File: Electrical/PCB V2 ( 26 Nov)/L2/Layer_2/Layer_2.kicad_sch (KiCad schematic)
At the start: 13 parts, among them SW1 SW_Push, U1 LM2596ADJ, U2 LM2596ADJ, U3 XT30UPB-M, U4 XT30UPB-M, U5 ESP32-S3-DEVKITM-1-N8, U6 XT30UPB-M, U7 XT30UPB-M, U8 XT30UPB-M, U9 XT30UPB-M

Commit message: ye
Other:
- note added: "Motor Controllers"
- note removed: "Motors"
- moved on the sheet: U3, U4, U5
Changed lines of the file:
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@@
 	)
 	(rectangle
-		(start 144.78 66.04)
-		(end 195.58 134.62)
+		(start 198.12 19.05)
+		(end 248.92 87.63)
 		(stroke
 			(width 0)
@@
 	)
 	(rectangle
-		(start 96.52 127)
-		(end 139.7 147.32)
+		(start 90.17 73.66)
+		(end 133.35 93.98)
 		(stroke
 			(width 0)
@@
 	(text "Coonector thing\n"
 		(exclude_from_sim no)
-		(at 116.586 122.936 0)
+		(at 110.236 69.596 0)
 		(effects
 			(font
@@
 		)
 	)
-	(text "Motors\n"
+	(text "Motor Controllers\n"
 		(exclude_from_sim no)
 		(at 130.556 20.828 0)
@@
 	(text "ESP32 for motor control\n"
 		(exclude_from_sim no)
-		(at 211.836 92.202 0)
+		(at 265.176 45.212 0)
 		(effects
 			(font
@@
 	)
 	(label "IN6"
-		(at 152.4 91.44 0)
+		(at 205.74 44.45 0)
 		(fields_autoplaced yes)
 		(effects
@@
 	)
 	(label "GND"
-		(at 152.4 129.54 0)
+		(at 205.74 82.55 0)
 		(fields_autoplaced yes)
 		(effects
@@
 	)
 	(label "IN8"
-		(at 152.4 96.52 0)
+		(at 205.74 49.53 0)
 		(fields_autoplaced yes)
 		(effects
@@
 	)
 	(label "IN1"
-		(at 152.4 78.74 0)
+		(at 205.74 31.75 0)
 		(fields_autoplaced yes)
 		(effects
@@
 	)
 	(label "3v3"
-		(at 152.4 76.2 0)
+		(at 205.74 29.21 0)
 		(fields_autoplaced yes)
 		(effects
@@
 	)
 	(label "3v3"
-		(at 133.35 138.43 0)
+		(at 127 85.09 0)
 		(fields_autoplaced yes)
 		(effects
@@
 	)
 	(label "IN7"
-		(at 152.4 93.98 0)
+		(at 205.74 46.99 0)
 		(fields_autoplaced yes)
 		(effects
@@
 	)
 	(label "GND"
-		(at 133.35 140.97 0)
+		(at 127 87.63 0)
 		(fields_autoplaced yes)
 		(effects
@@
 	)
 	(label "IN2"
-		(at 152.4 81.28 0)
+		(at 205.74 34.29 0)
 		(fields_autoplaced yes)
 		(effects
@@
 	)
 	(label "5v"
-		(at 114.3 139.7 0)
+		(at 107.95 86.36 0)
 		(fields_autoplaced yes)
 		(effects
@@
 	)
 	(label "IN3"
-		(at 152.4 83.82 0)
+		(at 205.74 36.83 0)
 		(fields_autoplaced yes)
 		(effects
@@
 	)
 	(label "GND"
-		(at 114.3 142.24 0)
+		(at 107.95 88.9 0)
 		(fields_autoplaced yes)
 		(effects
@@
 	)
 	(label "IN4"
-		(at 152.4 86.36 0)
+		(at 205.74 39.37 0)
 		(fields_autoplaced yes)
 		(effects
@@
 	)
 	(label "IN5"
-		(at 152.4 88.9 0)
+		(at 205.74 41.91 0)
 		(fields_autoplaced yes)
 		(effects
@@
 	(symbol
 		(lib_id "XT30UPB-M:XT30UPB-M")
-		(at 125.73 140.97 0)
+		(at 119.38 87.63 0)
 		(unit 1)
 		(exclude_from_sim no)
@@
 		(fields_autoplaced yes)
 		(property "Reference" "U4"
-			(at 126.365 130.81 0)
+			(at 120.015 77.47 0)
 			(effects
 				(font
@@
 		)
 		(property "Value" "XT30UPB-M"
-			(at 126.365 133.35 0)
+			(at 120.015 80.01 0)
 			(effects
 				(font
@@
 		)
 		(property "Footprint" "XT30UPB-M:XT30UPB-M"
-			(at 125.73 140.97 0)
+			(at 119.38 87.63 0)
 			(effects
 				(font
@@
 		)
 		(property "Datasheet" ""
-			(at 125.73 140.97 0)
+			(at 119.38 87.63 0)
 			(effects
 				(font
@@
 		)
 		(property "Description" ""
-			(at 125.73 140.97 0)
+			(at 119.38 87.63 0)
 			(effects
 				(font
@@
 		)
 		(property "MF" "amass"
-			(at 125.73 140.97 0)
+			(at 119.38 87.63 0)
 			(effects
 				(font
@@
 		)
 		(property "Description_1" "\n                        \n                            Socket; DC supply; XT30; male; PIN: 2; on PCBs; THT; yellow; 15A; 500V\n                        \n"
-			(at 125.73 140.97 0)
+			(at 119.38 87.63 0)
 			(effects
 				(font
@@
 		)
 		(property "Package" "None"
-			(at 125.73 140.97 0)
+			(at 119.38 87.63 0)
 			(effects
 				(font
@@
 		)
 		(property "Price" "None"
-			(at 125.73 140.97 0)
+			(at 119.38 87.63 0)
 			(effects
 				(font
@@
 		)
 		(property "SnapEDA_Link" "https://www.snapeda.com/parts/XT30UPB-M/AMASS/view-part/?ref=snap"
-			(at 125.73 140.97 0)
+			(at 119.38 87.63 0)
 			(effects
 				(font
@@
 		)
 		(property "MP" "XT30UPB-M"
-			(at 125.73 140.97 0)
+			(at 119.38 87.63 0)
 			(effects
 				(font
@@
 		)
 		(property "Availability" "Not in stock"
-			(at 125.73 140.97 0)
+			(at 119.38 87.63 0)
 			(effects
 				(font
@@
 		)
 		(property "Check_prices" "https://www.snapeda.com/parts/XT30UPB-M/AMASS/view-part/?ref=eda"
-			(at 125.73 140.97 0)
+			(at 119.38 87.63 0)
 			(effects
 				(font
@@
 	(symbol
 		(lib_id "ESP32-S3-DEVKITM-1-N8:ESP32-S3-DEVKITM-1-N8")
-		(at 172.72 104.14 0)
+		(at 226.06 57.15 0)
 		(unit 1)
 		(exclude_from_sim no)
@@
 		(fields_autoplaced yes)
 		(property "Reference" "U5"
-			(at 172.72 68.58 0)
+			(at 226.06 21.59 0)
 			(effects
 				(font
@@
 		)
 		(property "Value" "ESP32-S3-DEVKITM-1-N8"
-			(at 172.72 71.12 0)
+			(at 226.06 24.13 0)
 			(effects
 				(font
@@
 		)
 		(property "Footprint" "ESP32-S3-DEVKITM-1-N8:MODULE_ESP32-S3-DEVKITM-1-N8"
-			(at 172.72 104.14 0)
+			(at 226.06 57.15 0)
 			(effects
 				(font
@@
 		)
 		(property "Datasheet" ""
-			(at 172.72 104.14 0)
+			(at 226.06 57.15 0)
 			(effects
 				(font
@@
 		)
 		(property "Description" ""
-			(at 172.72 104.14 0)
+			(at 226.06 57.15 0)
 			(effects
 				(font
@@
 		)
 		(property "MF" "Espressif Systems"
-			(at 172.72 104.14 0)
+			(at 226.06 57.15 0)
 			(effects
 				(font
@@
 		)
 		(property "Description_1" "\n                        \n                            ESP32-S3-MINI-1-N8 ESP32-S Transceiver; 802.11 b/g/n (Wi-Fi, WiFi, WLAN), Bluetooth® 5.x (BLE) 2.4GHz Evaluation Board\n                        \n"
-			(at 172.72 104.14 0)
+			(at 226.06 57.15 0)
 			(effects
 				(font
@@
 		)
 		(property "Package" "None"
-			(at 172.72 104.14 0)
+			(at 226.06 57.15 0)
 			(effects
 				(font
@@
 		)
 		(property "Price" "None"
-			(at 172.72 104.14 0)
+			(at 226.06 57.15 0)
 			(effects
 				(font
@@
 		)
 		(property "Check_prices" "https://www.snapeda.com/parts/ESP32-S3-DEVKITM-1-N8/Espressif+Systems/view-part/?ref=eda"
-			(at 172.72 104.14 0)
+			(at 226.06 57.15 0)
 			(effects
 				(font
@@
 		)
 		(property "STANDARD" "Manufacturer Recommendations"
-			(at 172.72 104.14 0)
+			(at 226.06 57.15 0)
 			(effects
 				(font
@@
 		)
 		(property "PARTREV" "1.0"
-			(at 172.72 104.14 0)
+			(at 226.06 57.15 0)
 			(effects
 				(font
@@
 		)
 		(property "SnapEDA_Link" "https://www.snapeda.com/parts/ESP32-S3-DEVKITM-1-N8/Espressif+Systems/view-part/?ref=snap"
-			(at 172.72 104.14 0)
+			(at 226.06 57.15 0)
 			(effects
 				(font
@@
 		)
 		(property "MP" "ESP32-S3-DEVKITM-1-N8"
-			(at 172.72 104.14 0)
+			(at 226.06 57.15 0)
 			(effects
 				(font
@@
 		)
 		(property "Availability" "In Stock"
-			(at 172.72 104.14 0)
+			(at 226.06 57.15 0)
 			(effects
 				(font
@@
 		)
 		(property "MANUFACTURER" "Espressif Systems"
-			(at 172.72 104.14 0)
+			(at 226.06 57.15 0)
 			(effects
 				(font
@@
 	)
 	(symbol
-		(lib_name "motor driver:L298N")
 		(lib_id "motor driver:L298N")
 		(at 101.6 53.34 0)
@@
 	(symbol
 		(lib_id "XT30UPB-M:XT30UPB-M")
-		(at 106.68 142.24 0)
+		(at 100.33 88.9 0)
 		(unit 1)
 		(exclude_from_sim no)
@@
 		(fields_autoplaced yes)
 		(property "Reference" "U3"
-			(at 107.315 132.08 0)
+			(at 100.965 78.74 0)
 			(effects
 				(font
@@
 		)
 		(property "Value" "XT30UPB-M"
-			(at 107.315 134.62 0)
+			(at 100.965 81.28 0)
 			(effects
 				(font
@@
 		)
 		(property "Footprint" "XT30UPB-M:XT30UPB-M"
-			(at 106.68 142.24 0)
+			(at 100.33 88.9 0)
 			(effects
 				(font
@@
 		)
 		(property "Datasheet" ""
-			(at 106.68 142.24 0)
+			(at 100.33 88.9 0)
 			(effects
 				(font
@@
 		)
 		(property "Description" ""
-			(at 106.68 142.24 0)
+			(at 100.33 88.9 0)
 			(effects
 				(font
@@
 		)
 		(property "MF" "amass"
-			(at 106.68 142.24 0)
+			(at 100.33 88.9 0)
 			(effects
 				(font
@@
 		)
 		(property "Description_1" "\n                        \n                            Socket; DC supply; XT30; male; PIN: 2; on PCBs; THT; yellow; 15A; 500V\n                        \n"
-			(at 106.68 142.24 0)
+			(at 100.33 88.9 0)
 			(effects
 				(font
@@
 		)
 		(property "Package" "None"
-			(at 106.68 142.24 0)
+			(at 100.33 88.9 0)
 			(effects
 				(font
@@
 		)
 		(property "Price" "None"
-			(at 106.68 142.24 0)
+			(at 100.33 88.9 0)
 			(effects
 				(font
@@
 		)
 		(property "SnapEDA_Link" "https://www.snapeda.com/parts/XT30UPB-M/AMASS/view-part/?ref=snap"
-			(at 106.68 142.24 0)
+			(at 100.33 88.9 0)
 			(effects
 				(font
@@
 		)
 		(property "MP" "XT30UPB-M"
-			(at 106.68 142.24 0)
+			(at 100.33 88.9 0)
 			(effects
 				(font
@@
 		)
 		(property "Availability" "Not in stock"
-			(at 106.68 142.24 0)
+			(at 100.33 88.9 0)
 			(effects
 				(font
@@
 		)
 		(property "Check_prices" "https://www.snapeda.com/parts/XT30UPB-M/AMASS/view-part/?ref=eda"
-			(at 106.68 142.24 0)
-			(effects
-				(font
+			(at 100.33 88.9 0)
+			(effects
+				(font

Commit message: c f
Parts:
- L298N1, L298N2: footprint (none) -> l298n:TO127P2020X500X2100-15
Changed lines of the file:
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@@
 			)
 		)
-		(property "Footprint" ""
+		(property "Footprint" "l298n:TO127P2020X500X2100-15"
 			(at 118.11 30.226 0)
 			(effects
@@
 	)
 	(symbol
-		(lib_name "motor driver:L298N")
 		(lib_id "motor driver:L298N")
 		(at 140.97 52.07 0)
@@
 			)
 		)
-		(property "Footprint" ""
+		(property "Footprint" "l298n:TO127P2020X500X2100-15"
 			(at 157.48 28.956 0)
 			(effects

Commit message: dtdgdh
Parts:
- SW1: footprint (none) -> flipswitch:SW_100SP1T1B4M2QE
- U6, U7, U8, U9: footprint XT30UPB-M:XT30UPB-M -> xt30:XT30UPB-M
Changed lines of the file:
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@@
 			)
 		)
-		(property "Footprint" "XT30UPB-M:XT30UPB-M"
+		(property "Footprint" "xt30:XT30UPB-M"
 			(at 139.7 39.37 0)
 			(effects
@@
 			)
 		)
-		(property "Footprint" ""
+		(property "Footprint" "flipswitch:SW_100SP1T1B4M2QE"
 			(at 55.88 46.99 0)
 			(effects
@@
 			)
 		)
-		(property "Footprint" "XT30UPB-M:XT30UPB-M"
+		(property "Footprint" "xt30:XT30UPB-M"
 			(at 132.08 55.88 0)
 			(effects
@@
 			)
 		)
-		(property "Footprint" "XT30UPB-M:XT30UPB-M"
+		(property "Footprint" "xt30:XT30UPB-M"
 			(at 92.71 57.15 0)
 			(effects
@@
 			)
 		)
-		(property "Footprint" "XT30UPB-M:XT30UPB-M"
+		(property "Footprint" "xt30:XT30UPB-M"
 			(at 100.33 40.64 0)
 			(effects

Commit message: hehe
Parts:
- U1, U2: footprint LM2596ADJ:LM2596ADJ -> Motor Controller:LM2596ADJ
- U3, U4: footprint XT30UPB-M:XT30UPB-M -> xt30:XT30UPB-M
- U5: footprint ESP32-S3-DEVKITM-1-N8:MODULE_ESP32-S3-DEVKITM-1-N8 -> ESP32 DEV KIT:MODULE_ESP32-S3-DEVKITM-1-N8
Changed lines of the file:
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@@
 			)
 		)
-		(property "Footprint" "XT30UPB-M:XT30UPB-M"
+		(property "Footprint" "xt30:XT30UPB-M"
 			(at 119.38 87.63 0)
 			(effects
@@
 			)
 		)
-		(property "Footprint" "LM2596ADJ:LM2596ADJ"
+		(property "Footprint" "Motor Controller:LM2596ADJ"
 			(at 44.45 113.03 0)
 			(effects
@@
 			)
 		)
-		(property "Footprint" "ESP32-S3-DEVKITM-1-N8:MODULE_ESP32-S3-DEVKITM-1-N8"
+		(property "Footprint" "ESP32 DEV KIT:MODULE_ESP32-S3-DEVKITM-1-N8"
 			(at 226.06 57.15 0)
 			(effects
@@
 			)
 		)
-		(property "Footprint" "LM2596ADJ:LM2596ADJ"
+		(property "Footprint" "Motor Controller:LM2596ADJ"
 			(at 44.45 76.2 0)
 			(effects
@@
 			)
 		)
-		(property "Footprint" "XT30UPB-M:XT30UPB-M"
+		(property "Footprint" "xt30:XT30UPB-M"
 			(at 100.33 88.9 0)
 			(effects

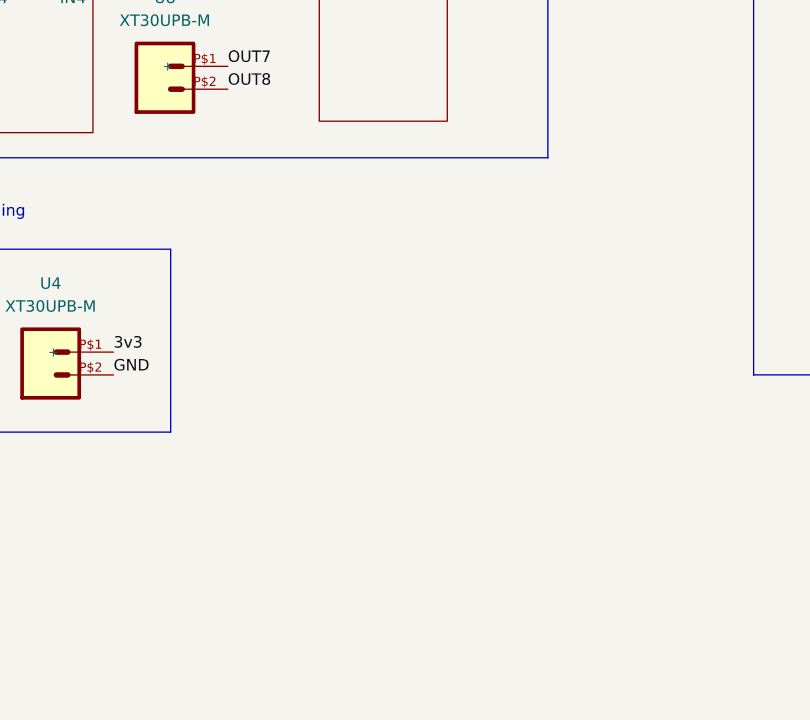
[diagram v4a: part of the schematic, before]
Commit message: xt30 added
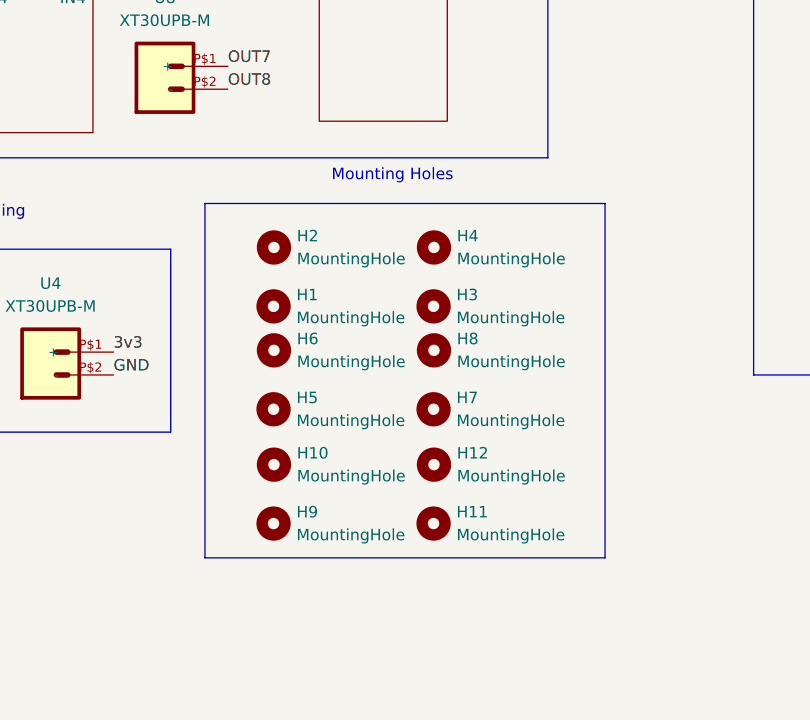
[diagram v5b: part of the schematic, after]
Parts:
- added H1, H10, H11, H12, H2, H3, H4, H5, H6, H7, H8, H9: MountingHole, MountingHole:MountingHole_3.2mm_M3_DIN965_Pad, symbol Mechanical:MountingHole
- U1, U2: footprint Motor Controller:LM2596ADJ -> LM2596ADJ:LM2596ADJ
- U3, U4: footprint xt30:XT30UPB-M -> XT30UPB-M:XT30UPB-M
- U5: footprint ESP32 DEV KIT:MODULE_ESP32-S3-DEVKITM-1-N8 -> ESP32-S3-DEVKITM-1-N8:MODULE_ESP32-S3-DEVKITM-1-N8
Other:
- note added: "Mounting Holes"

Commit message: concern
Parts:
- removed L298N1, L298N2: ~, l298n:TO127P2020X500X2100-15, symbol motor driver:L298N
- removed U8: XT30UPB-M, xt30:XT30UPB-M, symbol XT30UPB-M:XT30UPB-M
- added U10, U8: L298N, L298N:TO127P2020X500X2100-15, symbol l298n:L298N
- added U11: XT30UPB-M, xt30:XT30UPB-M, symbol XT30UPB-M:XT30UPB-M
- U3, U4: footprint XT30UPB-M:XT30UPB-M -> xt30:XT30UPB-M
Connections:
- net GND: now also U10.8 (GND), U8.8 (GND)
- net IN1: now also U8.5 (IN1)
- net IN2: now also U8.7 (IN2)
- net IN3: now also U8.10 (IN3)
- net IN4: now also U8.12 (IN4)
- net IN5: now also U10.5 (IN1)
- net IN6: now also U10.7 (IN2)
- net IN7: now also U10.10 (IN3)
- net IN8: now also U10.12 (IN4)
- net at U9.P$1 (+): now also U8.3 (OUT2)
- net at U9.P$2 (-): now also U8.2 (OUT1)
- net at U6.P$1 (+): now also U10.3 (OUT2)
- net at U6.P$2 (-): now also U10.2 (OUT1)
- net Out3: no longer names the net of U7.P$1 (+)
- net Out3: now also U10.14 (OUT4)
- net Out4: no longer names the net of U7.P$2 (-)
- net Out4: now also U10.13 (OUT3)
- new net: U11.P$1 (+), U8.14 (OUT4)
- new net: U11.P$2 (-), U8.13 (OUT3)
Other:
- moved on the sheet: U6, U7

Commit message: e
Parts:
- added J1: Conn_01x02, Connector_PinHeader_1.00mm:PinHeader_1x02_P1.00mm_Horizontal, symbol Connector_Generic:Conn_01x02
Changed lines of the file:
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@@
 	)
 	(label "GND"
-		(at 35.56 57.15 0)
+		(at 35.56 57.15 270)
 		(fields_autoplaced yes)
 		(effects
@@
 				(size 1.27 1.27)
 			)
-			(justify left bottom)
+			(justify right bottom)
 		)
 	)
@@
 					(unit 1)
 				)
+			)
+		)
+	)
+	(symbol
+		(lib_id "Connector_Generic:Conn_01x02")
+		(at 96.52 106.68 180)
+		(unit 1)
+		(exclude_from_sim no)
+		(in_bom yes)
+		(on_board yes)
+		(dnp no)
+		(fields_autoplaced yes)
+		(property "Reference" "J1"
+			(at 96.52 97.79 0)
+			(effects
+				(font
+					(size 1.27 1.27)
+				)
+			)
+		)
+		(property "Value" "Conn_01x02"
+			(at 96.52 100.33 0)
+			(effects
+				(font
+					(size 1.27 1.27)
+				)
+			)
+		)
+		(property "Footprint" "Connector_PinHeader_1.00mm:PinHeader_1x02_P1.00mm_Horizontal"
+			(at 96.52 106.68 0)
+			(effects
+				(font
+					(size 1.27 1.27)
+				)
+				(hide yes)
+			)
+		)
+		(property "Datasheet" "~"
+			(at 96.52 106.68 0)
+			(effects
+				(font
+					(size 1.27 1.27)
+				)
+				(hide yes)
+			)
+		)
+		(property "Description" "Generic connector, single row, 01x02, script generated (kicad-library-utils/schlib/autogen/connector/)"
+			(at 96.52 106.68 0)
+			(effects
+				(font
+					(size 1.27 1.27)
+				)
+				(hide yes)
+			)
+		)
+		(pin "1"
+		)
+		(pin "2"
+		)
+		(instances
+			(project "Layer_2"
+				(path "/164539e9-489b-4b17-b405-637c12a94360"
+					(reference "J1")
+					(unit 1)
+				)
